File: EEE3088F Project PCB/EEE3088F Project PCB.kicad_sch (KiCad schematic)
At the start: 2 parts

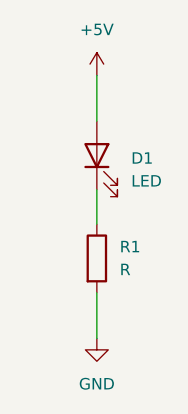
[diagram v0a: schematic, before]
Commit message: resistor in parallel
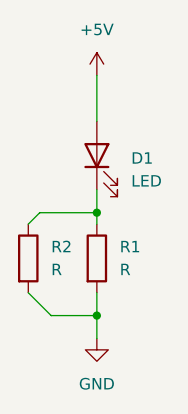
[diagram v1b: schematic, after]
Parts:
- added R2: R, symbol Device:R
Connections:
- net GND: now also R2.2
- net at D1.1 (K), R1.1: now also R2.1
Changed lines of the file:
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@@
 	(generator_version "9.0")
 	(paper "A4")
+	(junction
+		(at 55.88 101.6)
+		(diameter 0)
+		(color 0 0 0 0)
+	)
+	(junction
+		(at 55.88 90.17)
+		(diameter 0)
+		(color 0 0 0 0)
+	)
+	(wire
+		(pts
+			(xy 55.88 90.17) (xy 49.53 90.17)
+		)
+		(stroke
+			(width 0)
+			(type default)
+		)
+	)
 	(wire
 		(pts
@@
 	(wire
 		(pts
-			(xy 55.88 87.63) (xy 55.88 91.44)
-		)
-		(stroke
-			(width 0)
-			(type default)
-		)
-	)
-	(wire
-		(pts
-			(xy 55.88 99.06) (xy 55.88 104.14)
+			(xy 55.88 101.6) (xy 55.88 104.14)
+		)
+		(stroke
+			(width 0)
+			(type default)
+		)
+	)
+	(wire
+		(pts
+			(xy 49.53 90.17) (xy 48.26 91.44)
+		)
+		(stroke
+			(width 0)
+			(type default)
+		)
+	)
+	(wire
+		(pts
+			(xy 55.88 101.6) (xy 50.8 101.6)
+		)
+		(stroke
+			(width 0)
+			(type default)
+		)
+	)
+	(wire
+		(pts
+			(xy 55.88 87.63) (xy 55.88 90.17)
+		)
+		(stroke
+			(width 0)
+			(type default)
+		)
+	)
+	(wire
+		(pts
+			(xy 55.88 99.06) (xy 55.88 101.6)
+		)
+		(stroke
+			(width 0)
+			(type default)
+		)
+	)
+	(wire
+		(pts
+			(xy 55.88 90.17) (xy 55.88 91.44)
+		)
+		(stroke
+			(width 0)
+			(type default)
+		)
+	)
+	(wire
+		(pts
+			(xy 50.8 101.6) (xy 48.26 99.06)
 		)
 		(stroke
@@
 					(unit 1)
 				)
+			)
+		)
+	)
+	(symbol
+		(lib_id "Device:R")
+		(at 48.26 95.25 0)
+		(unit 1)
+		(exclude_from_sim no)
+		(in_bom yes)
+		(on_board yes)
+		(dnp no)
+		(fields_autoplaced yes)
+		(property "Reference" "R2"
+			(at 50.8 93.9799 0)
+			(effects
+				(font
+					(size 1.27 1.27)
+				)
+				(justify left)
+			)
+		)
+		(property "Value" "R"
+			(at 50.8 96.5199 0)
+			(effects
+				(font
+					(size 1.27 1.27)
+				)
+				(justify left)
+			)
+		)
+		(property "Footprint" ""
+			(at 46.482 95.25 90)
+			(effects
+				(font
+					(size 1.27 1.27)
+				)
+				(hide yes)
+			)
+		)
+		(property "Datasheet" "~"
+			(at 48.26 95.25 0)
+			(effects
+				(font
+					(size 1.27 1.27)
+				)
+				(hide yes)
+			)
+		)
+		(property "Description" "Resistor"
+			(at 48.26 95.25 0)
+			(effects
+				(font
+					(size 1.27 1.27)
+				)
+				(hide yes)
+			)
+		)
+		(pin "1"
+		)
+		(pin "2"
+		)
+		(instances
+			(project ""
+				(path "/e48caec1-c218-420e-929b-e5099c9fb7b6"
+					(reference "R2")
+					(unit 1)
+				)

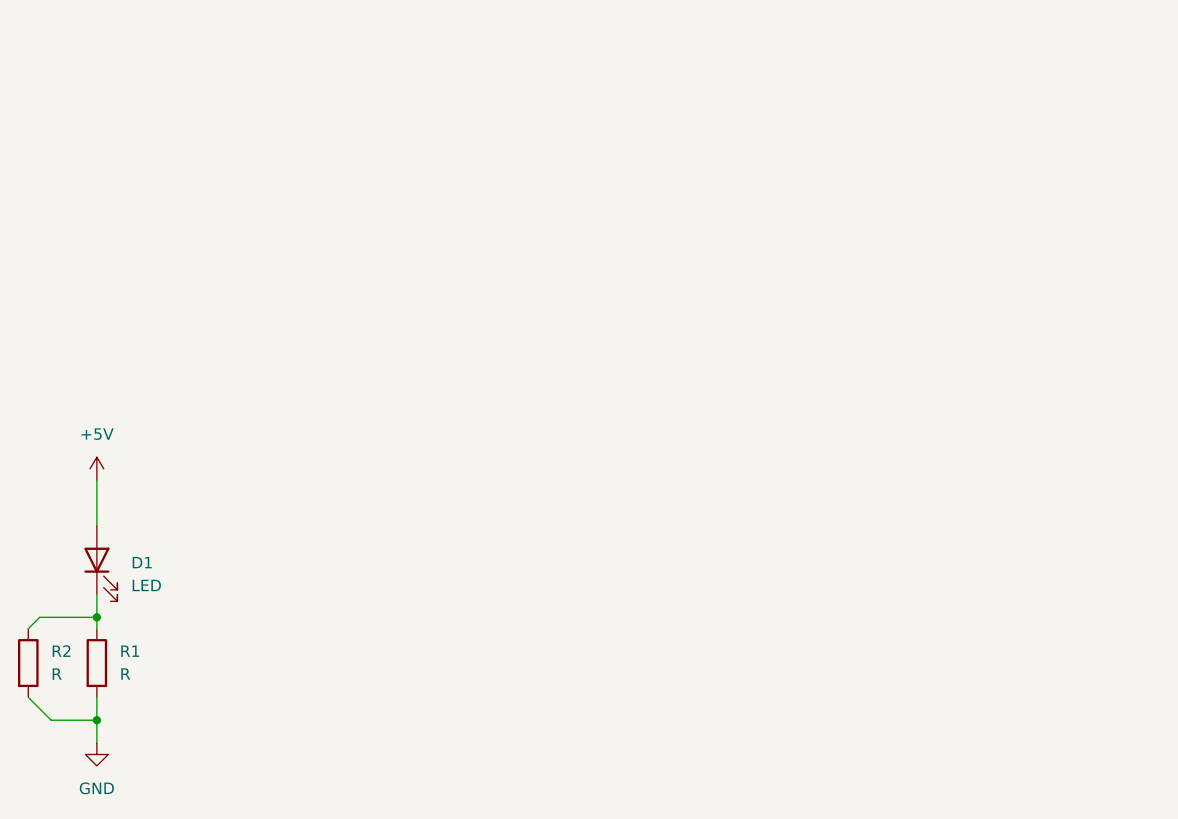
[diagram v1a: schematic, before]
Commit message: 2x16 pin connector & JST PH 2.00 connector
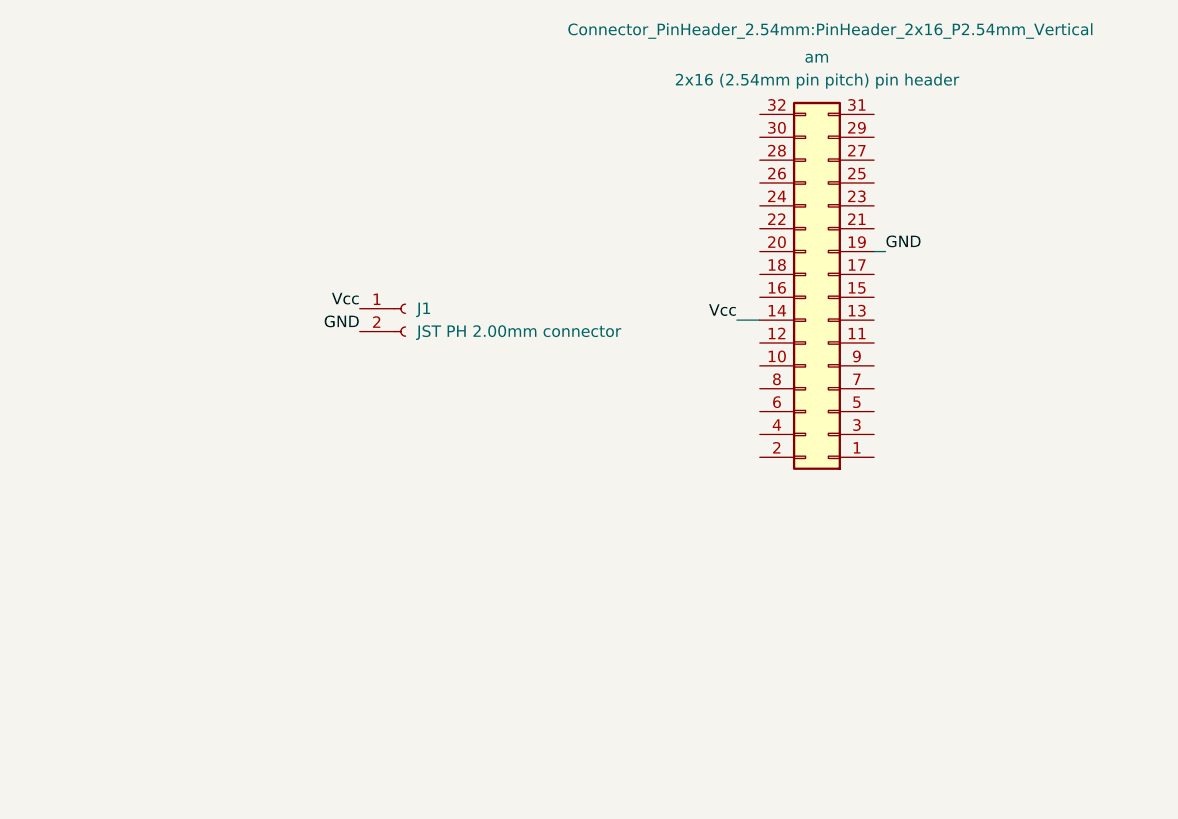
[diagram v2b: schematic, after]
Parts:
- removed D1: LED, symbol Device:LED
- removed R1, R2: R, symbol Device:R
- added J1: JST PH 2.00mm connector, Connector_JST:JST_PH_S2B-PH-K_1x02_P2.00mm_Horizontal, symbol Connector:Conn_01x02_Socket
- added am: 2x16 (2.54mm pin pitch) pin header, Connector_PinHeader_2.54mm:PinHeader_2x16_P2.54mm_Vertical, symbol Connector_Generic:Conn_02x16_Odd_Even
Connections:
- net GND: now also J1.2 (Pin_2), am.19 (Pin_19)
- new net Vcc: J1.1 (Pin_1), am.14 (Pin_14)
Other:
- title: (none) -> MM Power PCB

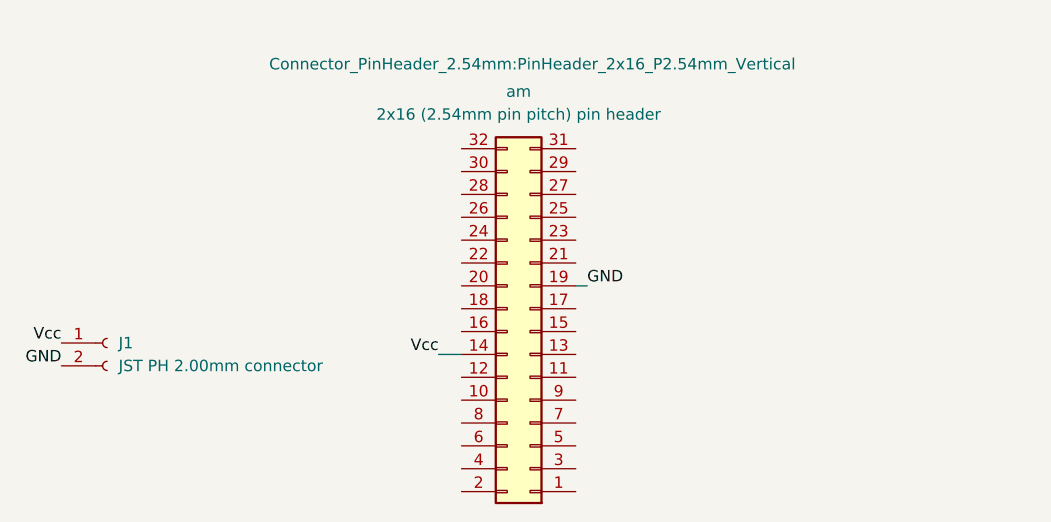
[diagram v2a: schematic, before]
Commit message: added pin net labels to connectors
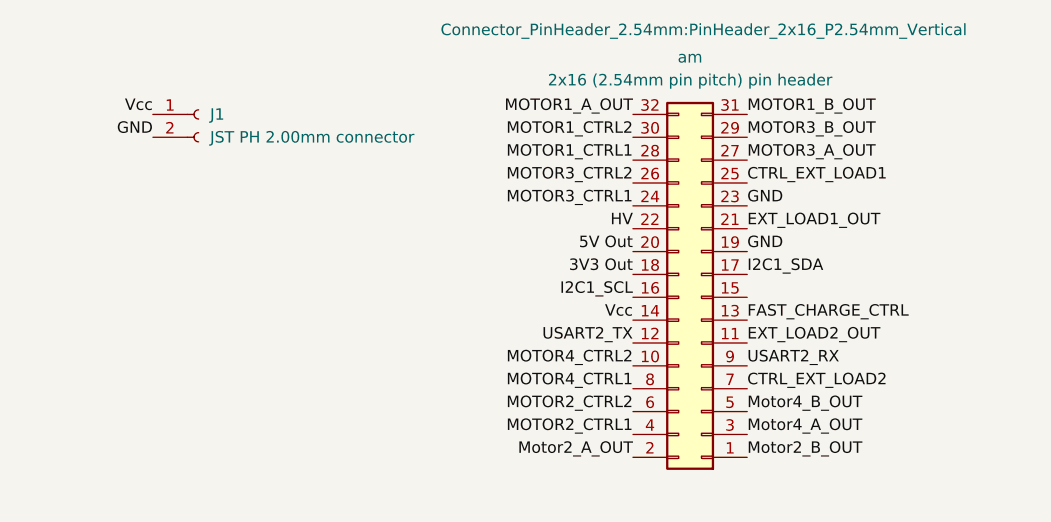
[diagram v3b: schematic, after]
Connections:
- net GND: now also am.23 (Pin_23)
- net Motor2_B_OUT: now reaches am.1 (Pin_1)
- net MOTOR4_CTRL2: now reaches am.10 (Pin_10)
- net EXT_LOAD2_OUT: now reaches am.11 (Pin_11)
- net USART2_TX: now reaches am.12 (Pin_12)
- net FAST_CHARGE_CTRL: now reaches am.13 (Pin_13)
- net I2C1_SCL: now reaches am.16 (Pin_16)
- net I2C1_SDA: now reaches am.17 (Pin_17)
- net 3V3 Out: now reaches am.18 (Pin_18)
- net Motor2_A_OUT: now reaches am.2 (Pin_2)
- net 5V Out: now reaches am.20 (Pin_20)
- net EXT_LOAD1_OUT: now reaches am.21 (Pin_21)
- net HV: now reaches am.22 (Pin_22)
- net MOTOR3_CTRL1: now reaches am.24 (Pin_24)
- net CTRL_EXT_LOAD1: now reaches am.25 (Pin_25)
- net MOTOR3_CTRL2: now reaches am.26 (Pin_26)
- net MOTOR3_A_OUT: now reaches am.27 (Pin_27)
- net MOTOR1_CTRL1: now reaches am.28 (Pin_28)
- net MOTOR3_B_OUT: now reaches am.29 (Pin_29)
- net Motor4_A_OUT: now reaches am.3 (Pin_3)
- net MOTOR1_CTRL2: now reaches am.30 (Pin_30)
- net MOTOR1_B_OUT: now reaches am.31 (Pin_31)
- net MOTOR1_A_OUT: now reaches am.32 (Pin_32)
- net MOTOR2_CTRL1: now reaches am.4 (Pin_4)
- net Motor4_B_OUT: now reaches am.5 (Pin_5)
- net MOTOR2_CTRL2: now reaches am.6 (Pin_6)
- net CTRL_EXT_LOAD2: now reaches am.7 (Pin_7)
- net MOTOR4_CTRL1: now reaches am.8 (Pin_8)
- net USART2_RX: now reaches am.9 (Pin_9)
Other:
- moved on the sheet: J1, am

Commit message: added a calaculations section, and my motor driver circuit
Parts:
- added C1, C6: 0.01uF, symbol Device:C
- added C2, C4: 2.2uF, symbol Device:C
- added C3, C5: 10uF, symbol Device:C
- added R_ISENSE_1, R_ISENSE_2: 0.4, symbol Device:R
- added R_ISENSE_3, R_ISENSE_4: 1, symbol Device:R
- added U1: DRV8833PWR, Package_SO:HTSSOP-16-1EP_4.4x5mm_P0.65mm_EP3.4x5mm_Mask2.46x2.31mm_ThermalVias, symbol Driver_Motor:DRV8833PWP
- added U2: DRV8833PWPR, Package_SO:HTSSOP-16-1EP_4.4x5mm_P0.65mm_EP3.4x5mm_Mask2.46x2.31mm_ThermalVias, symbol Driver_Motor:DRV8833PWP
- renumbered am to am1
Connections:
- net GND: now also C2.1, C3.1, C4.1, C5.1, R_ISENSE_1.1, R_ISENSE_2.1, R_ISENSE_3.1, R_ISENSE_4.1, U1.13 (GND), U1.17 (GND), U2.13 (GND), U2.17 (GND); no longer J1.2 (Pin_2)
- net MOTOR1_A_OUT: now also U1.2 (AOUT1)
- net MOTOR1_B_OUT: now also U1.4 (AOUT2)
- net MOTOR1_CTRL1: now also U1.16 (AIN1)
- net MOTOR1_CTRL2: now also U1.15 (AIN2)
- net MOTOR2_CTRL1: now also U1.9 (BIN1)
- net MOTOR2_CTRL2: now also U1.10 (BIN2)
- net MOTOR3_A_OUT: now also U2.2 (AOUT1)
- net MOTOR3_B_OUT: now also U2.4 (AOUT2)
- net MOTOR3_CTRL1: now also U2.16 (AIN1)
- net MOTOR3_CTRL2: now also U2.15 (AIN2)
- net MOTOR4_CTRL1: now also U2.9 (BIN1)
- net MOTOR4_CTRL2: now also U2.10 (BIN2)
- net Motor2_A_OUT: now also U1.7 (BOUT1)
- net Motor2_B_OUT: now also U1.5 (BOUT2)
- net Motor4_A_OUT: now also U2.7 (BOUT1)
- net Motor4_B_OUT: now also U2.5 (BOUT2)
- new net: C1.2, U1.11 (VCP)
- new net: R_ISENSE_2.2, U1.6 (BISEN)
- new net: R_ISENSE_1.2, U1.3 (AISEN)
- new net: C6.2, U2.11 (VCP)
- new net: C4.2, U2.14 (VINT)
- new net: R_ISENSE_4.2, U2.6 (BISEN)
- new net: C2.2, U1.14 (VINT)
- new net: R_ISENSE_3.2, U2.3 (AISEN)
- new net VM: C1.1, C3.2, C5.2, C6.1, U1.12 (VM), U2.12 (VM)
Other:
- note added: "1. R_ISENSE_1 = R_ISENSE_2 = 200mV/500mA = 0.4 Ohms 2. R_ISENSE_3 = R_ISENSE_4 = 200mV/200mA = 1 Ohms"
- note added: "CALCULATIONS"
- note added: "MOTOR DRIVER"
- note added: "PIN CONNECTORS AND BATTERY CONNECTOR"
- moved on the sheet: J1, am1
